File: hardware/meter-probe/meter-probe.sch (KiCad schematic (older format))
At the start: 16 parts, among them J1 Main Board, Q1 BSS138, SW1 Sensor Button, U1 RT9193, U2 TCS3472, U3 P82B96

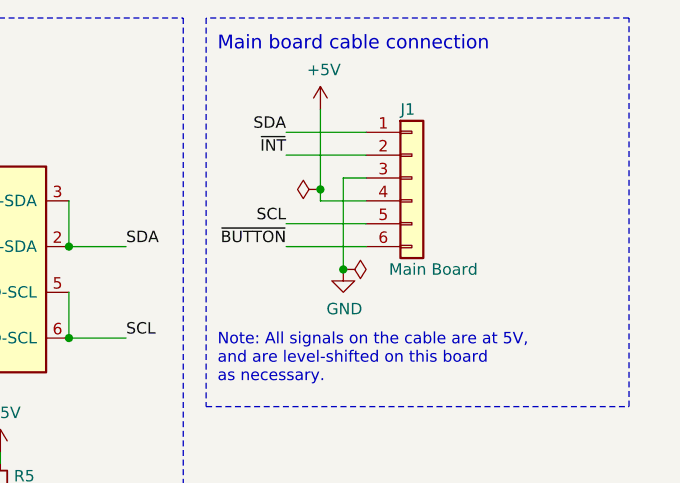
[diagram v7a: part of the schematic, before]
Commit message: Added 10uF capacitor to +5V input on meter PCB
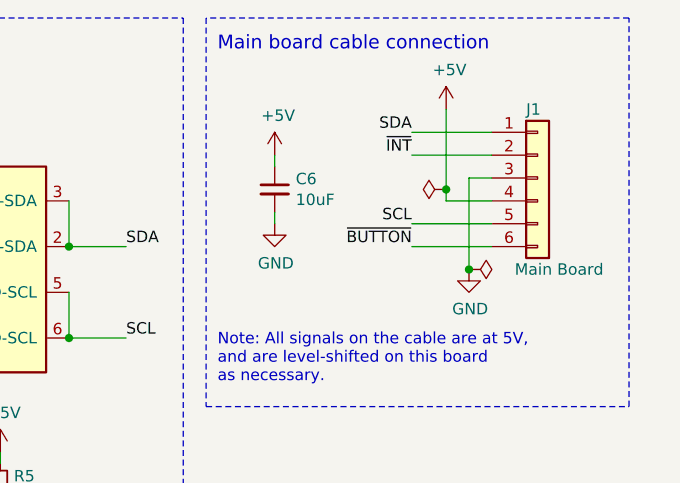
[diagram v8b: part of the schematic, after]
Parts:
- added C6: 10uF, Capacitor_SMD:C_0805_2012Metric, symbol Device:C_Small
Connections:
- net +5V: now also C6.1
- net GND: now also C6.2
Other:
- moved on the sheet: J1
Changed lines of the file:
@@
 L Connector_Generic:Conn_01x06 J1
 U 1 1 5F8CB1BB
-P 6000 1550
-F 0 "J1" H 5950 1850 50  0000 L CNN
-F 1 "Main Board" H 5900 1150 50  0000 L CNN
-F 2 "lib_fp:SolderWire-0.1sqmm_1x06_Cable" H 6000 1550 50  0001 C CNN
-F 3 "~" H 6000 1550 50  0001 C CNN
-F 4 "WIRE-TO-BOARD" H 6000 1550 50  0001 C CNN "Description"
-	1    6000 1550
-	1    0    0    -1
-$EndComp
-$Comp
-L power:+5V #PWR0112
-U 1 1 5F922946
-P 5600 1250
-F 0 "#PWR0112" H 5600 1100 50  0001 C CNN
-F 1 "+5V" H 5615 1423 50  0000 C CNN
-F 2 "" H 5600 1250 50  0001 C CNN
-F 3 "" H 5600 1250 50  0001 C CNN
-	1    5600 1250
-	1    0    0    -1
-$EndComp
-$Comp
-L power:GND #PWR0113
-U 1 1 5F922E28
-P 5700 1950
-F 0 "#PWR0113" H 5700 1700 50  0001 C CNN
-F 1 "GND" H 5705 1777 50  0000 C CNN
-F 2 "" H 5700 1950 50  0001 C CNN
-F 3 "" H 5700 1950 50  0001 C CNN
-	1    5700 1950
+P 6550 1550
+F 0 "J1" H 6500 1850 50  0000 L CNN
+F 1 "Main Board" H 6450 1150 50  0000 L CNN
+F 2 "lib_fp:SolderWire-0.1sqmm_1x06_Cable" H 6550 1550 50  0001 C CNN
+F 3 "~" H 6550 1550 50  0001 C CNN
+F 4 "WIRE-TO-BOARD" H 6550 1550 50  0001 C CNN "Description"
+	1    6550 1550
 	1    0    0    -1
 $EndComp
@@
 $EndComp
 Wire Wire Line
-	5800 1550 5700 1550
-Wire Wire Line
-	5700 1550 5700 1950
-Wire Wire Line
-	5600 1250 5600 1600
-Wire Wire Line
-	5600 1650 5800 1650
-Text Label 5450 1350 2    50   ~ 0
+	6350 1550 6250 1550
+Wire Wire Line
+	6250 1550 6250 1950
+Wire Wire Line
+	6150 1650 6350 1650
+Text Label 6000 1350 2    50   ~ 0
 SDA
-Text Label 5450 1450 2    50   ~ 0
+Text Label 6000 1450 2    50   ~ 0
 ~INT
-Text Label 5450 1750 2    50   ~ 0
+Text Label 6000 1750 2    50   ~ 0
 SCL
-Text Label 5450 1850 2    50   ~ 0
+Text Label 6000 1850 2    50   ~ 0
 ~BUTTON
 Wire Wire Line
-	5450 1350 5800 1350
-Wire Wire Line
-	5450 1450 5800 1450
-Wire Wire Line
-	5450 1750 5800 1750
-Wire Wire Line
-	5450 1850 5800 1850
+	6000 1350 6350 1350
+Wire Wire Line
+	6000 1450 6350 1450
+Wire Wire Line
+	6000 1750 6350 1750
+Wire Wire Line
+	6000 1850 6350 1850
 $Comp
 L Device:R_Small R4
@@
 	5000 850  5000 3450
 $Comp
+L power:PWR_FLAG #FLG0102
+U 1 1 5F98ABC8
+P 6250 1950
+F 0 "#FLG0102" H 6250 2025 50  0001 C CNN
+F 1 "PWR_FLAG" V 6250 2077 50  0001 L CNN
+F 2 "" H 6250 1950 50  0001 C CNN
+F 3 "~" H 6250 1950 50  0001 C CNN
+	1    6250 1950
+	0    1    1    0
+$EndComp
+$Comp
+L Device:C_Small C6
+U 1 1 5F9A840E
+P 5400 1600
+F 0 "C6" H 5492 1646 50  0000 L CNN
+F 1 "10uF" H 5492 1555 50  0000 L CNN
+F 2 "Capacitor_SMD:C_0805_2012Metric" H 5400 1600 50  0001 C CNN
+F 3 "https://media.digikey.com/pdf/Data%20Sheets/Samsung%20PDFs/CL_Series_MLCC_ds.pdf" H 5400 1600 50  0001 C CNN
+F 4 "CAP CER 10UF 16V X5R 0805" H 5400 1600 50  0001 C CNN "Description"
+F 5 "Samsung Electro-Mechanics" H 5400 1600 50  0001 C CNN "Manufacturer"
+F 6 "CL21A106KOQNNNG" H 5400 1600 50  0001 C CNN "Manufacturer PN"
+F 7 "Digi-Key" H 5400 1600 50  0001 C CNN "Supplier"
+F 8 "1276-6455-1-ND" H 5400 1600 50  0001 C CNN "Supplier PN"
+	1    5400 1600
+	1    0    0    -1
+$EndComp
+Wire Wire Line
+	6150 1600 6150 1650
+Connection ~ 6150 1600
+$Comp
 L power:PWR_FLAG #FLG0101
 U 1 1 5F9890D6
-P 5600 1600
-F 0 "#FLG0101" H 5600 1675 50  0001 C CNN
-F 1 "PWR_FLAG" V 5600 1727 50  0001 L CNN
-F 2 "" H 5600 1600 50  0001 C CNN
-F 3 "~" H 5600 1600 50  0001 C CNN
-	1    5600 1600
+P 6150 1600
+F 0 "#FLG0101" H 6150 1675 50  0001 C CNN
+F 1 "PWR_FLAG" V 6150 1727 50  0001 L CNN
+F 2 "" H 6150 1600 50  0001 C CNN
+F 3 "~" H 6150 1600 50  0001 C CNN
+	1    6150 1600
 	0    -1   -1   0
 $EndComp
-Connection ~ 5600 1600
-Wire Wire Line
-	5600 1600 5600 1650
-$Comp
-L power:PWR_FLAG #FLG0102
-U 1 1 5F98ABC8
-P 5700 1950
-F 0 "#FLG0102" H 5700 2025 50  0001 C CNN
-F 1 "PWR_FLAG" V 5700 2077 50  0001 L CNN
-F 2 "" H 5700 1950 50  0001 C CNN
-F 3 "~" H 5700 1950 50  0001 C CNN
-	1    5700 1950
-	0    1    1    0
-$EndComp
-Connection ~ 5700 1950
+Wire Wire Line
+	6150 1250 6150 1600
+Connection ~ 6250 1950
+$Comp
+L power:GND #PWR0113
+U 1 1 5F922E28
+P 6250 1950
+F 0 "#PWR0113" H 6250 1700 50  0001 C CNN
+F 1 "GND" H 6255 1777 50  0000 C CNN
+F 2 "" H 6250 1950 50  0001 C CNN
+F 3 "" H 6250 1950 50  0001 C CNN
+	1    6250 1950
+	1    0    0    -1
+$EndComp
+$Comp
+L power:+5V #PWR0112
+U 1 1 5F922946
+P 6150 1250
+F 0 "#PWR0112" H 6150 1100 50  0001 C CNN
+F 1 "+5V" H 6165 1423 50  0000 C CNN
+F 2 "" H 6150 1250 50  0001 C CNN
+F 3 "" H 6150 1250 50  0001 C CNN
+	1    6150 1250
+	1    0    0    -1
+$EndComp
+$Comp
+L power:+5V #PWR?
+U 1 1 5F9B4A6D
+P 5400 1450
+F 0 "#PWR?" H 5400 1300 50  0001 C CNN
+F 1 "+5V" H 5415 1623 50  0000 C CNN
+F 2 "" H 5400 1450 50  0001 C CNN
+F 3 "" H 5400 1450 50  0001 C CNN
+	1    5400 1450
+	1    0    0    -1
+$EndComp
+$Comp
+L power:GND #PWR?
+U 1 1 5F9B4E8D
+P 5400 1750
+F 0 "#PWR?" H 5400 1500 50  0001 C CNN
+F 1 "GND" H 5405 1577 50  0000 C CNN
+F 2 "" H 5400 1750 50  0001 C CNN
+F 3 "" H 5400 1750 50  0001 C CNN
+	1    5400 1750
+	1    0    0    -1
+$EndComp
+Wire Wire Line
+	5400 1700 5400 1750
+Wire Wire Line
+	5400 1450 5400 1500
 $EndSCHEMATC
